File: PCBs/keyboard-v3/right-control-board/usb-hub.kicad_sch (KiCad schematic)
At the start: 16 parts, among them U101 USB2534-1080AEN, U801 NCP380HMU05AATBG, Y101 CX2016SA24000D0HLLG3

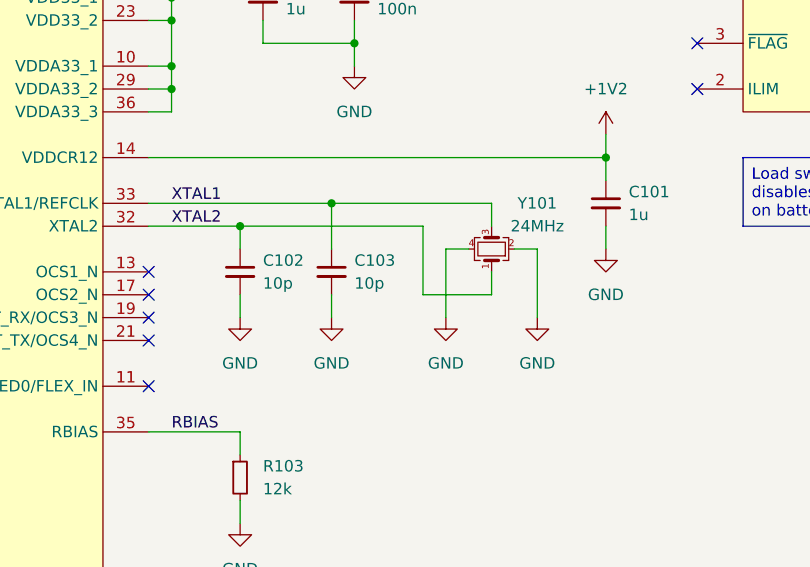
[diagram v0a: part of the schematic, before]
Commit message: Right control board placement and schematic done
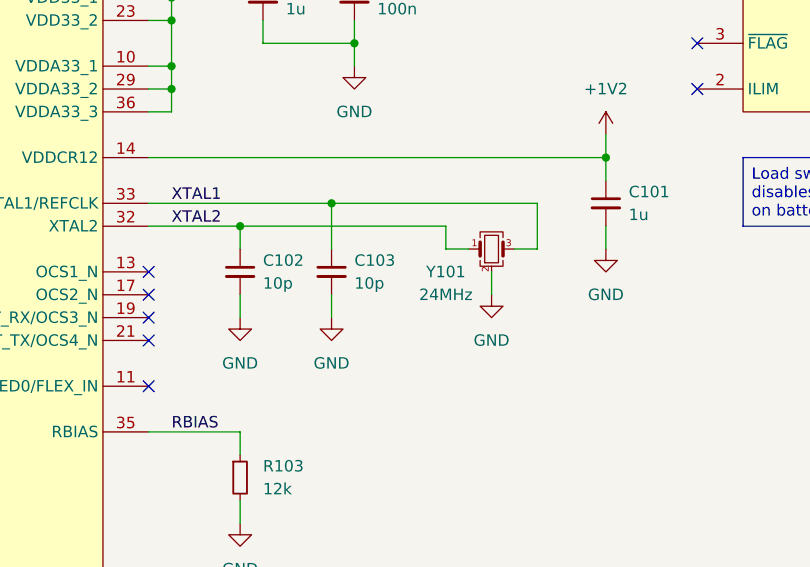
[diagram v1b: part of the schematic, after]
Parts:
- U101: footprint QFN50P600X600X100-37N-D -> project_footprints:QFN50P600X600X100-37N-D
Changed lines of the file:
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@@
 	(wire
 		(pts
-			(xy 187.96 88.9) (xy 185.42 88.9)
+			(xy 154.94 53.34) (xy 154.94 55.88)
 		)
 		(stroke
@@
 	(wire
 		(pts
-			(xy 154.94 53.34) (xy 154.94 55.88)
+			(xy 195.58 88.9) (xy 193.04 88.9)
 		)
 		(stroke
@@
 	(wire
 		(pts
-			(xy 182.88 93.98) (xy 190.5 93.98)
-		)
-		(stroke
-			(width 0)
-			(type default)
-		)
-	)
-	(wire
-		(pts
 			(xy 40.64 111.76) (xy 43.18 111.76)
 		)
@@
 	(wire
 		(pts
-			(xy 185.42 88.9) (xy 185.42 96.52)
-		)
-		(stroke
-			(width 0)
-			(type default)
-		)
-	)
-	(wire
-		(pts
 			(xy 43.18 71.12) (xy 43.18 68.58)
 		)
@@
 	(wire
 		(pts
-			(xy 162.56 86.36) (xy 182.88 86.36)
+			(xy 162.56 86.36) (xy 185.42 86.36)
 		)
 		(stroke
@@
 	(wire
 		(pts
-			(xy 195.58 88.9) (xy 193.04 88.9)
-		)
-		(stroke
-			(width 0)
-			(type default)
-		)
-	)
-	(wire
-		(pts
 			(xy 76.2 76.2) (xy 91.44 76.2)
 		)
@@
 	(wire
 		(pts
-			(xy 182.88 86.36) (xy 182.88 93.98)
-		)
-		(stroke
-			(width 0)
-			(type default)
-		)
-	)
-	(wire
-		(pts
 			(xy 203.2 78.74) (xy 203.2 76.2)
 		)
@@
 	(wire
 		(pts
+			(xy 195.58 83.82) (xy 195.58 88.9)
+		)
+		(stroke
+			(width 0)
+			(type default)
+		)
+	)
+	(wire
+		(pts
 			(xy 175.26 55.88) (xy 213.36 55.88)
 		)
@@
 	(wire
 		(pts
-			(xy 172.72 83.82) (xy 190.5 83.82)
+			(xy 172.72 83.82) (xy 195.58 83.82)
 		)
 		(stroke
@@
 	(wire
 		(pts
+			(xy 185.42 88.9) (xy 187.96 88.9)
+		)
+		(stroke
+			(width 0)
+			(type default)
+		)
+	)
+	(wire
+		(pts
 			(xy 53.34 99.06) (xy 53.34 101.6)
 		)
@@
 	(wire
 		(pts
-			(xy 246.38 71.12) (xy 243.84 71.12)
+			(xy 185.42 86.36) (xy 185.42 88.9)
 		)
 		(stroke
@@
 	(wire
 		(pts
-			(xy 195.58 96.52) (xy 195.58 88.9)
+			(xy 246.38 71.12) (xy 243.84 71.12)
 		)
 		(stroke
@@
 	(wire
 		(pts
-			(xy 190.5 93.98) (xy 190.5 91.44)
+			(xy 165.1 63.5) (xy 165.1 66.04)
 		)
 		(stroke
@@
 	(wire
 		(pts
-			(xy 165.1 63.5) (xy 165.1 66.04)
+			(xy 162.56 86.36) (xy 162.56 88.9)
 		)
 		(stroke
@@
 	(wire
 		(pts
-			(xy 162.56 86.36) (xy 162.56 88.9)
+			(xy 246.38 73.66) (xy 246.38 71.12)
 		)
 		(stroke
@@
 	(wire
 		(pts
-			(xy 246.38 73.66) (xy 246.38 71.12)
+			(xy 190.5 91.44) (xy 190.5 93.98)
 		)
 		(stroke
@@
 	(wire
 		(pts
-			(xy 190.5 83.82) (xy 190.5 86.36)
-		)
-		(stroke
-			(width 0)
-			(type default)
-		)
-	)
-	(wire
-		(pts
 			(xy 43.18 99.06) (xy 53.34 99.06)
 		)
@@
 	)
 	(symbol
-		(lib_id "power:GND")
-		(at 185.42 96.52 0)
-		(unit 1)
-		(exclude_from_sim no)
-		(in_bom yes)
-		(on_board yes)
-		(dnp no)
-		(fields_autoplaced yes)
-		(property "Reference" "#PWR0123"
-			(at 185.42 102.87 0)
-			(effects
-				(font
-					(size 1.27 1.27)
-				)
-				(hide yes)
-			)
-		)
-		(property "Value" "GND"
-			(at 185.42 101.6 0)
-			(effects
-				(font
-					(size 1.27 1.27)
-				)
-			)
-		)
-		(property "Footprint" ""
-			(at 185.42 96.52 0)
-			(effects
-				(font
-					(size 1.27 1.27)
-				)
-				(hide yes)
-			)
-		)
-		(property "Datasheet" ""
-			(at 185.42 96.52 0)
-			(effects
-				(font
-					(size 1.27 1.27)
-				)
-				(hide yes)
-			)
-		)
-		(property "Description" "Power symbol creates a global label with name \"GND\" , ground"
-			(at 185.42 96.52 0)
-			(effects
-				(font
-					(size 1.27 1.27)
-				)
-				(hide yes)
-			)
-		)
-		(pin "1"
-		)
-		(instances
-			(project "right-control-board"
-				(path "/982f1c46-f6d6-42a2-bf2a-9fb0e913f11f/9e40c337-fa3a-418a-a06f-f29c5aeab638"
-					(reference "#PWR0123")
-					(unit 1)
-				)
-			)
-		)
-	)
-	(symbol
 		(lib_id "PWR-SYM:+3V3_USB")
 		(at 43.18 96.52 0)
@@
 	(symbol
 		(lib_id "Device:Crystal_GND24_Small")
-		(at 190.5 88.9 90)
+		(at 190.5 88.9 0)
 		(unit 1)
 		(exclude_from_sim no)
@@
 		(dnp no)
 		(property "Reference" "Y101"
-			(at 195.58 83.82 90)
+			(at 185.42 91.44 0)
 			(effects
 				(font
@@
 		)
 		(property "Value" "CX2016SA24000D0HLLG3"
-			(at 195.58 86.36 90)
+			(at 193.04 93.98 90)
 			(effects
 				(font
@@
 		)
 		(property "Frequency" "24MHz"
-			(at 195.58 86.36 90)
+			(at 185.42 93.98 0)
 			(effects
 				(font
@@
 			)
 		)
-		(property "Footprint" "QFN50P600X600X100-37N-D"
+		(property "Footprint" "project_footprints:QFN50P600X600X100-37N-D"
 			(at 121.92 147.32 0)
 			(effects
@@
 	(symbol
 		(lib_id "power:GND")
-		(at 195.58 96.52 0)
+		(at 190.5 93.98 0)
 		(unit 1)
 		(exclude_from_sim no)
@@
 		(fields_autoplaced yes)
 		(property "Reference" "#PWR0124"
-			(at 195.58 102.87 0)
+			(at 190.5 100.33 0)
 			(effects
 				(font
@@
 		)
 		(property "Value" "GND"
-			(at 195.58 101.6 0)
+			(at 190.5 99.06 0)
 			(effects
 				(font
@@
 		)
 		(property "Footprint" ""
-			(at 195.58 96.52 0)
+			(at 190.5 93.98 0)
 			(effects
 				(font
@@
 		)
 		(property "Datasheet" ""
-			(at 195.58 96.52 0)
+			(at 190.5 93.98 0)
 			(effects
 				(font
@@
 		)
 		(property "Description" "Power symbol creates a global label with name \"GND\" , ground"
-			(at 195.58 96.52 0)
+			(at 190.5 93.98 0)
 			(effects
 				(font

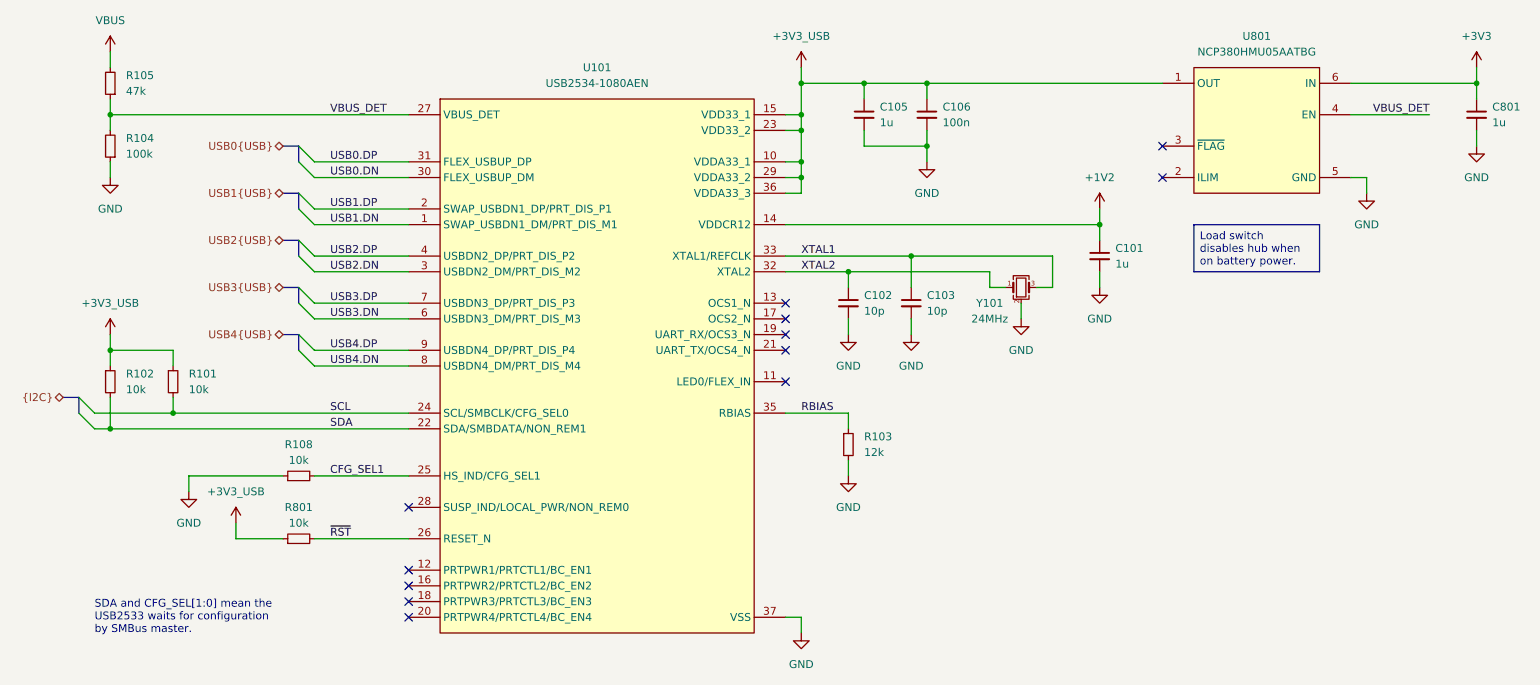
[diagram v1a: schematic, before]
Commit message: Added mounting holes
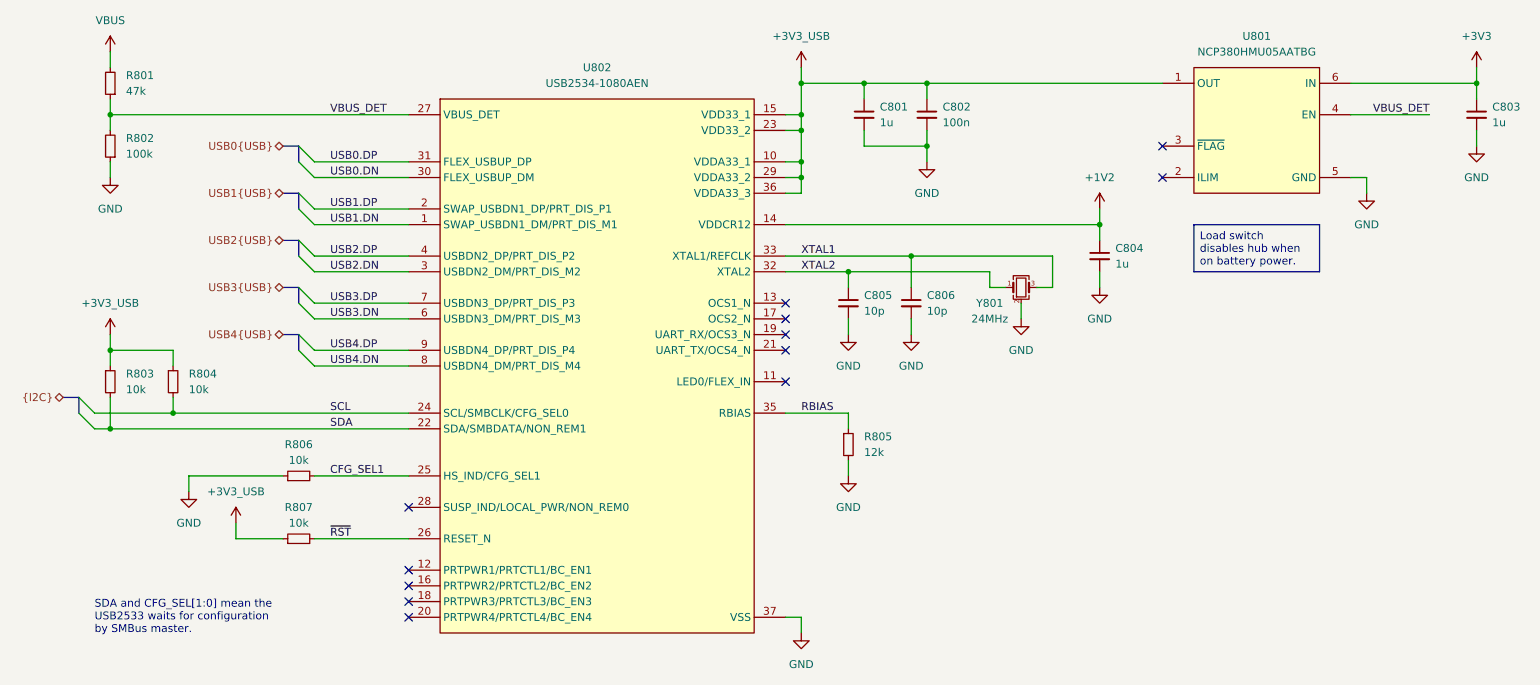
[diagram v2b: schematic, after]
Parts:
- renumbered C105 to C801, C106 to C802, C801 to C803, C101 to C804, C102 to C805, C103 to C806, R105 to R801, R104 to R802, R102 to R803, R101 to R804, R103 to R805, R108 to R806, R801 to R807, U101 to U802, Y101 to Y801
